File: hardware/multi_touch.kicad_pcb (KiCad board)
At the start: 2 copper layers, 25 x 30 mm, 18 parts, among them P1 CON-SENSOR, P2 CONN_12, U1 M24C64, U2 MPR121Q, U3 DRILL, U4 DRILL, U5 DRILL, U6 DRILL

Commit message: drc run, change drills to np
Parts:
- U3, U4, U5, U6: footprint DRILL_NP -> kicad-libraries:DRILL_NP

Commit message: fix fiducials
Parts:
- Fiducial_Mark (x2): footprint Fiducial_Mark -> kicad-libraries:Fiducial_Mark

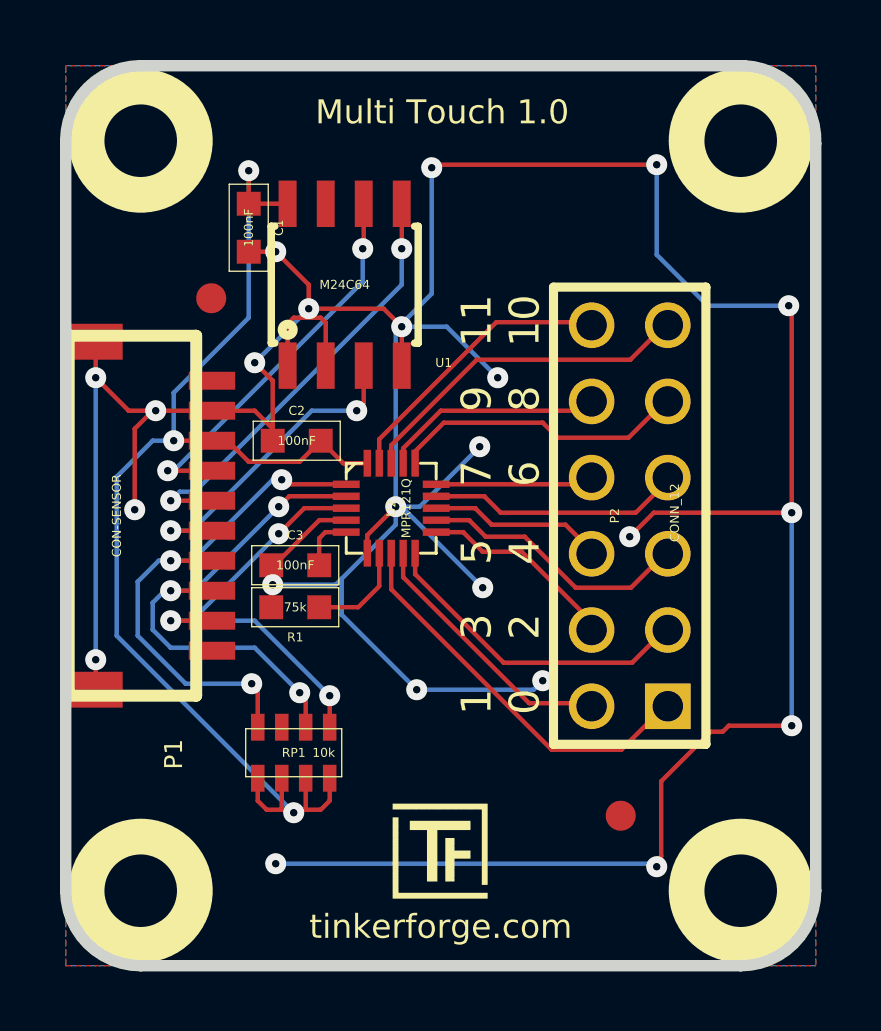
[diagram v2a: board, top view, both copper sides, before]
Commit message: Add 3d information
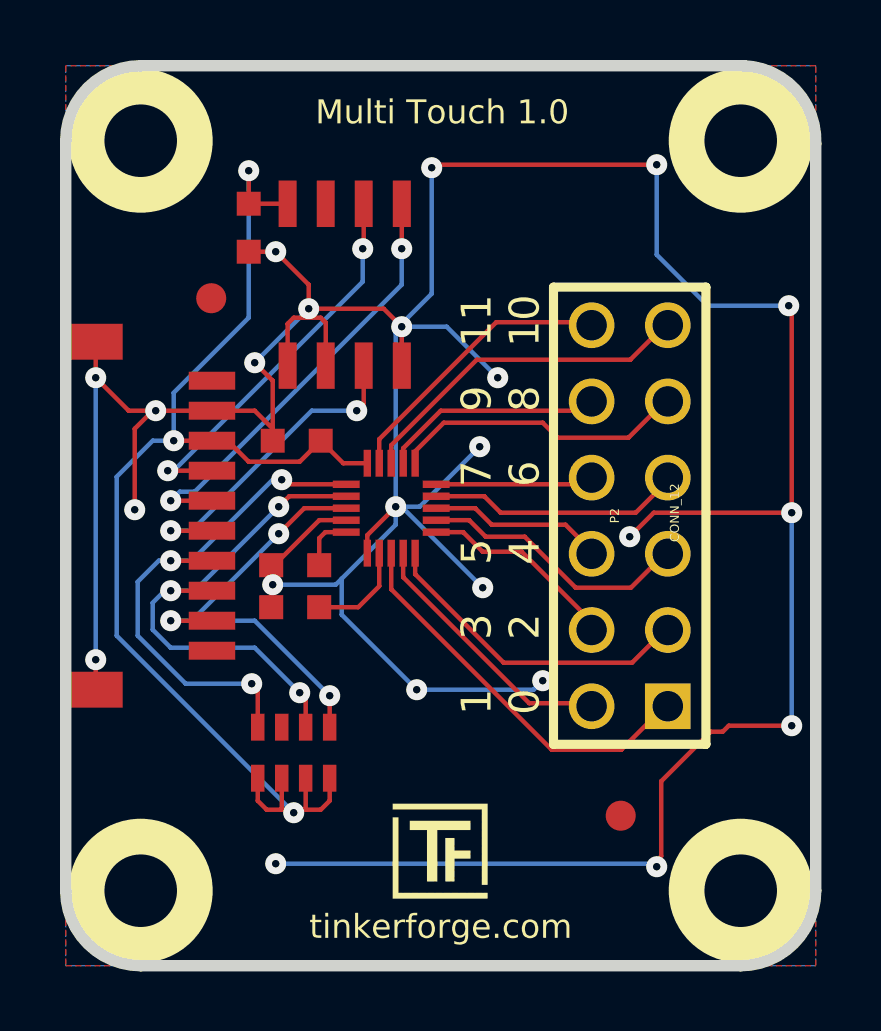
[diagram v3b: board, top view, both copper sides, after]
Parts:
- C1, C2, C3: footprint 0603 -> kicad-libraries:C0603
- G***: footprint Logo_31x31 -> kicad-libraries:Logo_31x31
- P1: footprint CON-SENSOR -> kicad-libraries:CON-SENSOR
- R1: footprint 0603 -> kicad-libraries:R0603
- RP1: footprint 0603X4 -> kicad-libraries:0603X4
- U1: footprint SOIC8 -> kicad-libraries:SOIC8
- U2: footprint QFN20-3X3 -> kicad-libraries:QFN20-3X3
- VAL: footprint WEEE_7mm -> kicad-libraries:WEEE_7mm
- VAL: footprint CE_5mm -> kicad-libraries:CE_5mm
- turned VAL to 0 degrees
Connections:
- P1 pad 1: (no net) -> Net-(P1-Pad1)
- P1 pad 10: (no net) -> Net-(P1-Pad10)
- RP1 pad 3: (no net) -> Net-(RP1-Pad3)
- U1 pad 7: (no net) -> Net-(U1-Pad7)
